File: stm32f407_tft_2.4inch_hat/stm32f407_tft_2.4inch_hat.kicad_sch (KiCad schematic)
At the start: 6 parts, among them P1 STM32F407-DISC P1, P2 STM32F407-DISC P2, U1 TFT SPI 240x320

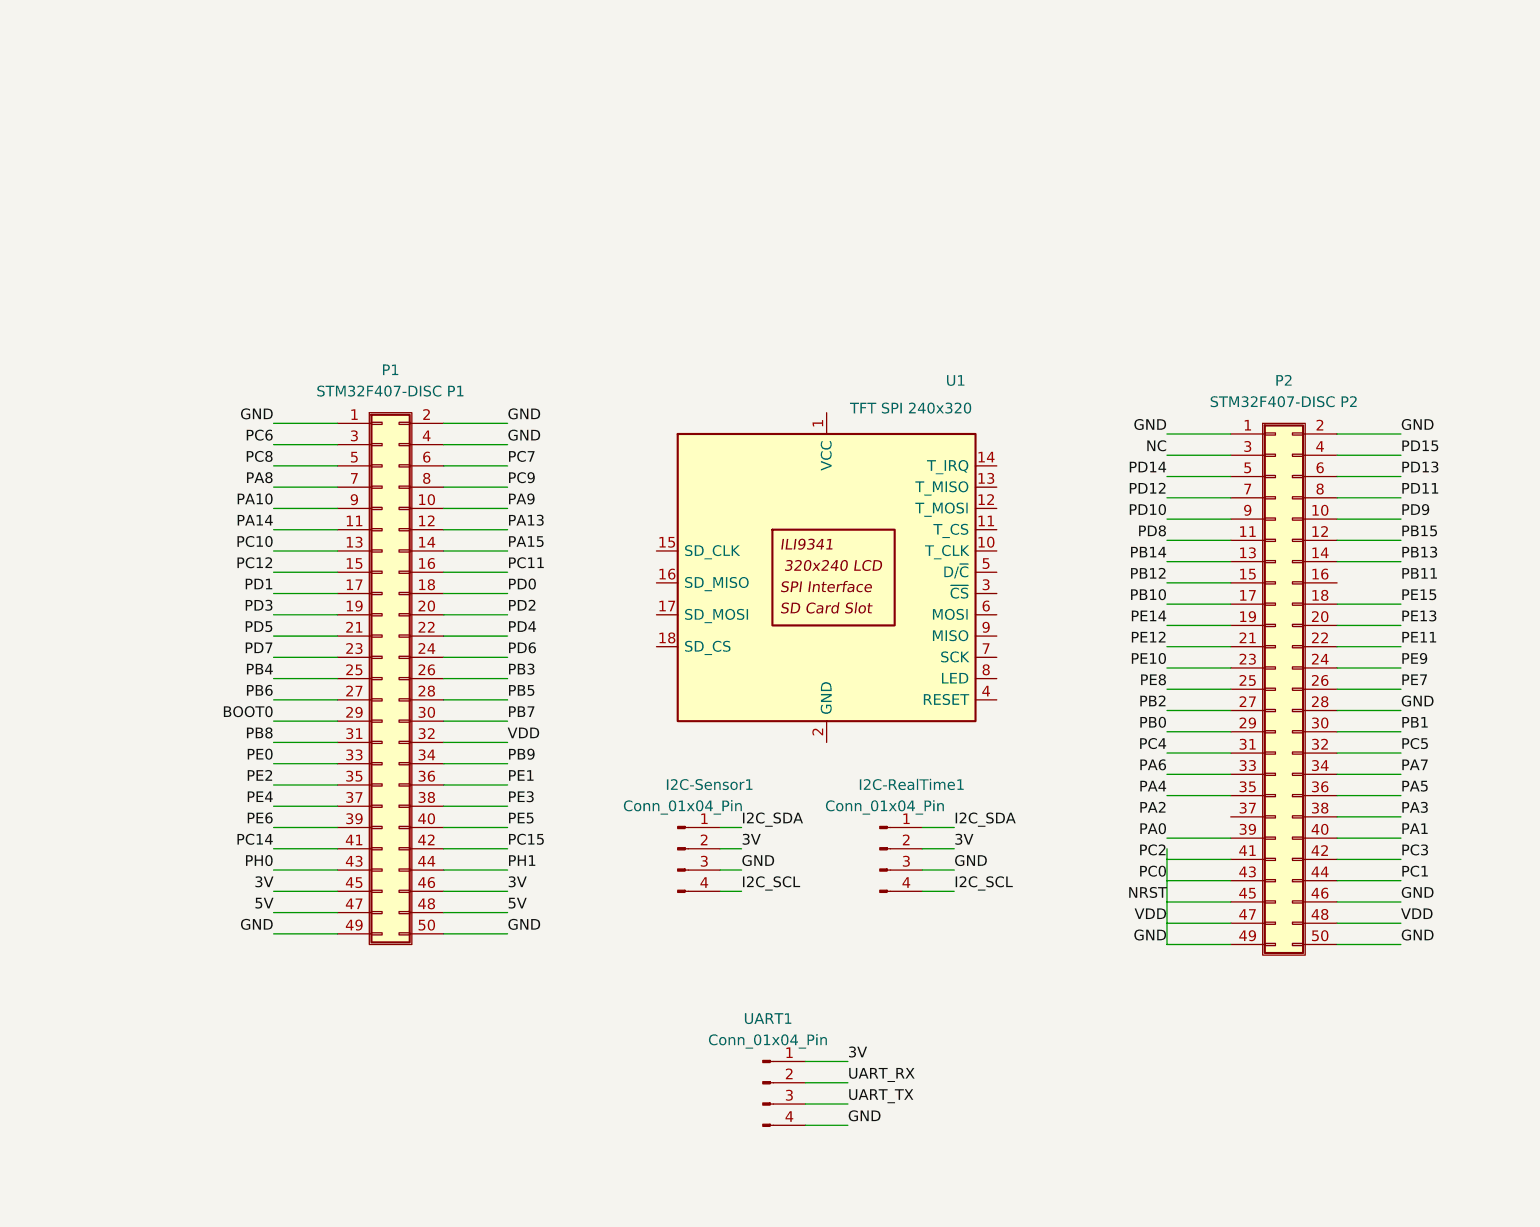
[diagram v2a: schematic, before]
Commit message: Wire i2c2 and tft
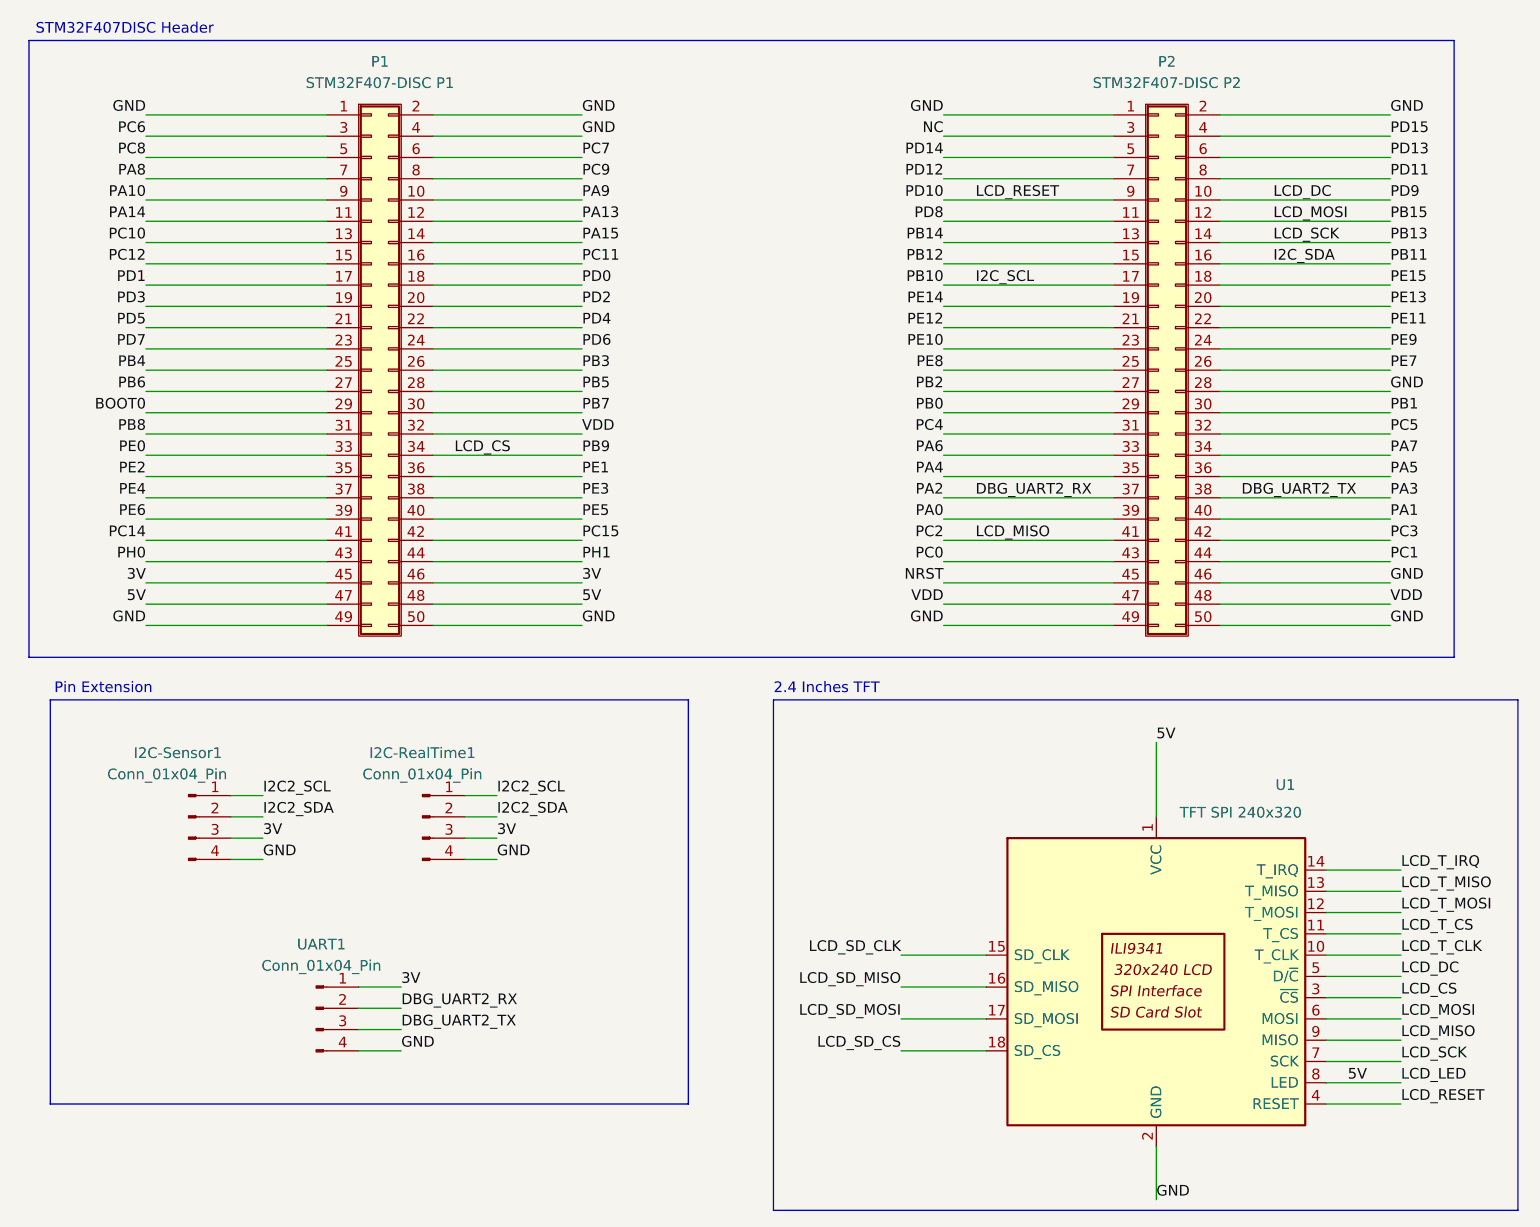
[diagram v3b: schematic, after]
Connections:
- net PB10 is gone; now on net I2C_SCL: P2.17 (PA6)
- net PB13 is gone; now on net LCD_SCK: P2.14 (PA3)
- net PB15 is gone; now on net LCD_MOSI: P2.12 (PA1)
- net PB9 is gone; now on net LCD_CS: P1.34 (PD0)
- net PD10 is gone; now on net LCD_RESET: P2.9 (PC2)
- net PD9 is gone; now on net LCD_DC: P2.10 (PC3)
- net UART_RX is gone; now on net DBG_UART2_RX: UART1.2 (Pin_2)
- net UART_TX is gone; now on net DBG_UART2_TX: UART1.3 (Pin_3)
- net 3V: now also I2C-RealTime1.3 (Pin_3), I2C-Sensor1.3 (Pin_3); no longer I2C-RealTime1.2 (Pin_2), I2C-Sensor1.2 (Pin_2)
- net 5V: now also U1.1 (VCC), U1.8 (LED)
- net GND: now also I2C-RealTime1.4 (Pin_4), I2C-Sensor1.4 (Pin_4), U1.2 (GND); no longer I2C-RealTime1.3 (Pin_3), I2C-Sensor1.3 (Pin_3), P1.32 (PD2), P2.41 (PD10), P2.43 (PD12), P2.45 (PD14), P2.47 (NC), P2.48 (PD15)
- net I2C_SCL: no longer I2C-RealTime1.4 (Pin_4), I2C-Sensor1.4 (Pin_4)
- net I2C_SDA: now also P2.16 (PA5); no longer I2C-RealTime1.1 (Pin_1), I2C-Sensor1.1 (Pin_1)
- net LCD_T_CLK: now reaches U1.10 (T_CLK)
- net LCD_T_CS: now reaches U1.11 (T_CS)
- net LCD_T_MOSI: now reaches U1.12 (T_MOSI)
- net LCD_T_MISO: now reaches U1.13 (T_MISO)
- net LCD_T_IRQ: now reaches U1.14 (T_IRQ)
- net LCD_SD_CLK: now reaches U1.15 (SD_CLK)
- net LCD_SD_MISO: now reaches U1.16 (SD_MISO)
- net LCD_SD_MOSI: now reaches U1.17 (SD_MOSI)
- net LCD_SD_CS: now reaches U1.18 (SD_CS)
- net LCD_CS: now reaches U1.3 (~{CS})
- net LCD_RESET: now reaches U1.4 (RESET)
- net LCD_DC: now reaches U1.5 (D/~{C})
- net LCD_MOSI: now reaches U1.6 (MOSI)
- net LCD_SCK: now reaches U1.7 (SCK)
- net LCD_MISO: now reaches U1.9 (MISO)
- net LCD_MISO: now also P2.41 (PD10)
- net DBG_UART2_RX: now reaches P2.37 (PB14)
- net PA3 renamed DBG_UART2_TX
- new net I2C2_SCL: I2C-RealTime1.1 (Pin_1), I2C-Sensor1.1 (Pin_1)
- new net I2C2_SDA: I2C-RealTime1.2 (Pin_2), I2C-Sensor1.2 (Pin_2)
- new net NRST: P2.45 (PD14)
- new net PC0: P2.43 (PD12)
- new net VDD: P1.32 (PD2), P2.47 (NC), P2.48 (PD15)
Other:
- note added: "2.4 Inches TFT"
- note added: "Pin Extension"
- note added: "STM32F407DISC Header"
- moved on the sheet: I2C-RealTime1, I2C-Sensor1, P1, P2, U1, UART1

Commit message: Fix pinout pcb & sch are not correct
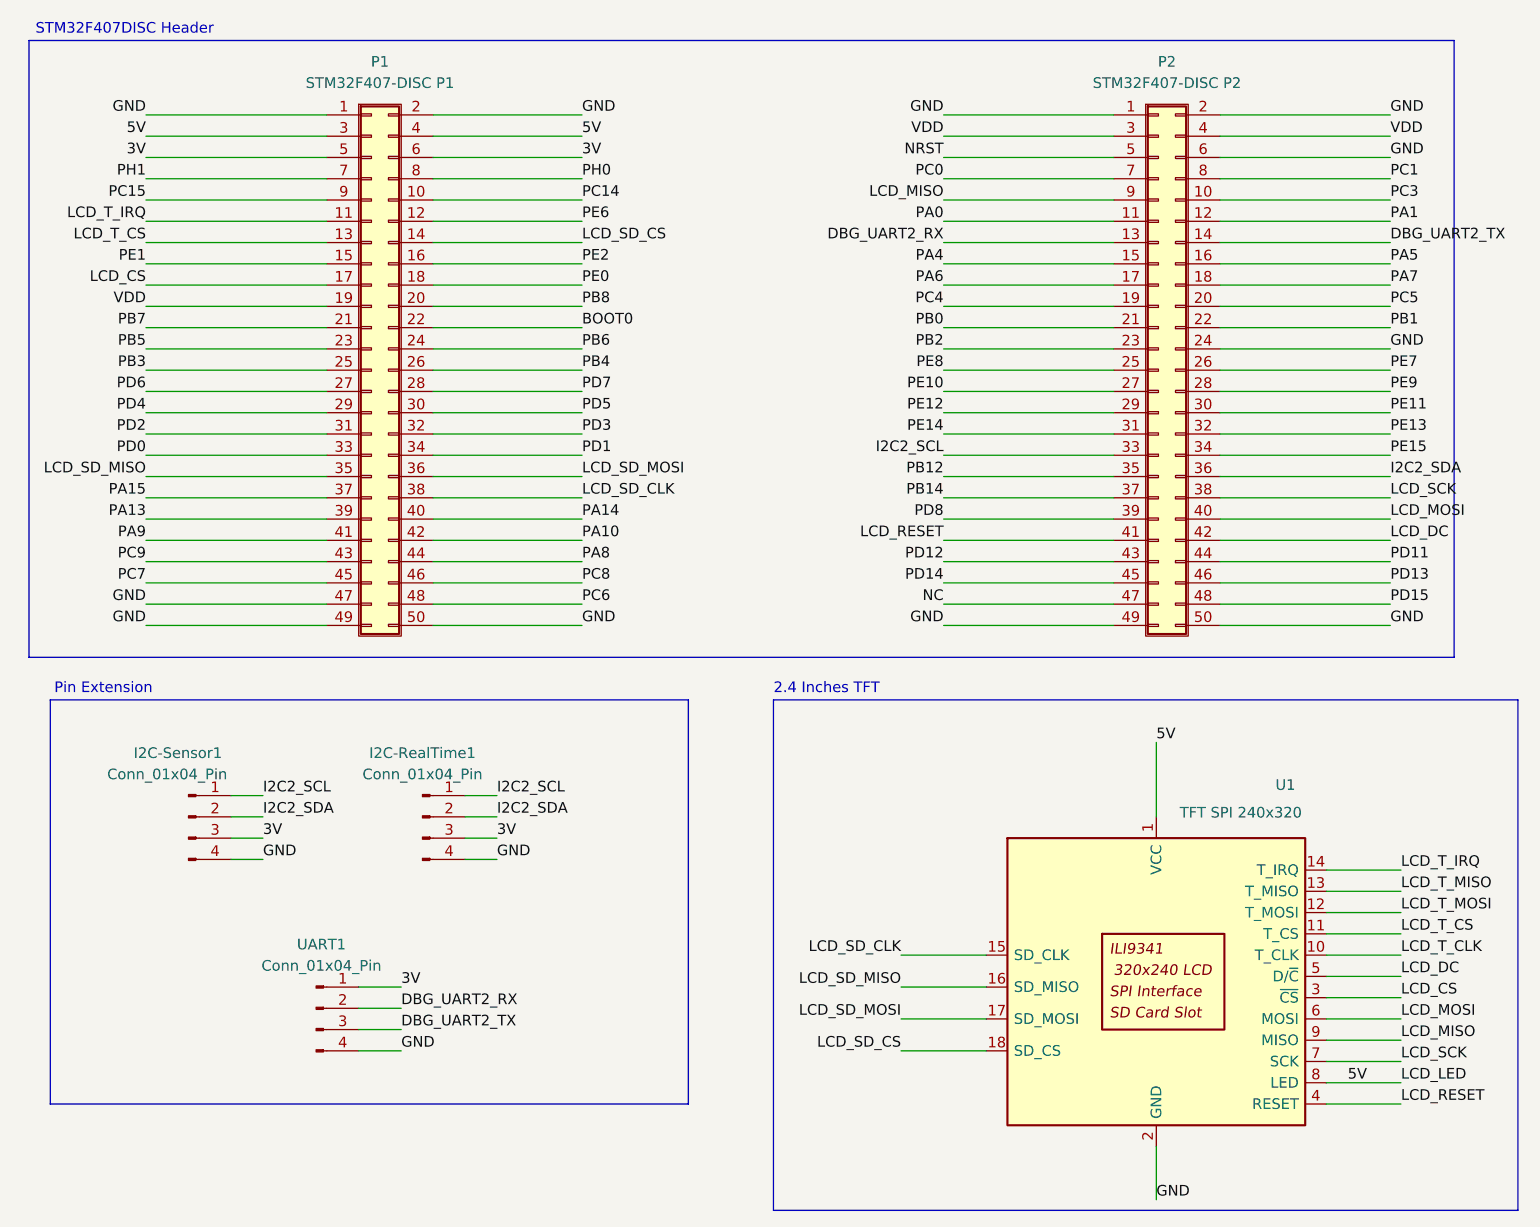
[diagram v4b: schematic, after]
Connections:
- net I2C_SCL is gone; now on net PA6: P2.17 (PA6)
- net I2C_SDA is gone; now on net PA5: P2.16 (PA5)
- net PC10 is gone; now on net LCD_T_CS: P1.13 (PE4)
- net PC11 is gone; now on net PE2: P1.16 (PE1)
- net PC12 is gone; now on net PE1: P1.15 (PE2)
- net PE3 is gone; now on net LCD_SD_CLK: P1.38 (PA15)
- net PE4 is gone; now on net PA15: P1.37 (PC10)
- net PE5 is gone; now on net PA14: P1.40 (PA13)
- net 3V: now also P1.5 (3V), P1.6 (3V); no longer P1.45 (PC8), P1.46 (PC7)
- net 5V: now also P1.3 (5V), P1.4 (5V); no longer P1.47 (PC6), P1.48 (GND)
- net BOOT0: now also P1.22 (PB7); no longer P1.29 (PD5)
- net DBG_UART2_RX: now also P2.13 (PA2); no longer P2.37 (PB14)
- net DBG_UART2_TX: now also P2.14 (PA3); no longer P2.38 (PB13)
- net GND: now also P1.47 (PC6), P2.24 (GND), P2.6 (GND); no longer P1.4 (5V), P2.28 (PE9), P2.46 (PD13)
- net I2C2_SCL: now also P2.33 (PB10)
- net I2C2_SDA: now also P2.36 (PB11)
- net LCD_CS: now also P1.17 (PE0); no longer P1.34 (PD0)
- net LCD_DC: now also P2.42 (PD9); no longer P2.10 (PC3)
- net LCD_MISO: now also P2.9 (PC2); no longer P2.41 (PD10)
- net LCD_MOSI: now also P2.40 (PB15); no longer P2.12 (PA1)
- net LCD_RESET: now also P2.41 (PD10); no longer P2.9 (PC2)
- net LCD_SCK: now also P2.38 (PB13); no longer P2.14 (PA3)
- net LCD_SD_CS: now also P1.14 (PE3)
- net LCD_SD_MISO: now also P1.35 (PC12)
- net LCD_SD_MOSI: now also P1.36 (PC11)
- net LCD_T_IRQ: now also P1.11 (PE6)
- net NC: now also P2.47 (NC); no longer P2.3 (VDD)
- net NRST: now also P2.5 (NRST); no longer P2.45 (PD14)
- net PA0: now also P2.11 (PA0); no longer P2.39 (PD8)
- net PA1: now also P2.12 (PA1); no longer P2.40 (PB15)
- net PA10: now also P1.42 (PA9); no longer P1.9 (PC14)
- net PA13: now also P1.39 (PA14); no longer P1.12 (PE5)
- net PA14: no longer P1.11 (PE6)
- net PA15: no longer P1.14 (PE3)
- net PA4: now also P2.15 (PA4); no longer P2.35 (PB12)
- net PA5: no longer P2.36 (PB11)
- net PA6: no longer P2.33 (PB10)
- net PA7: now also P2.18 (PA7); no longer P2.34 (PE15)
- net PA8: now also P1.44 (PC9); no longer P1.7 (PH0)
- net PA9: now also P1.41 (PA10); no longer P1.10 (PC15)
- net PB0: now also P2.21 (PB0); no longer P2.29 (PE12)
- net PB1: now also P2.22 (PB1); no longer P2.30 (PE11)
- net PB12: now also P2.35 (PB12); no longer P2.15 (PA4)
- net PB14: now also P2.37 (PB14); no longer P2.13 (PA2)
- net PB2: now also P2.23 (PB2); no longer P2.27 (PE10)
- net PB3: now also P1.25 (PB4); no longer P1.26 (PB3)
- net PB4: now also P1.26 (PB3); no longer P1.25 (PB4)
- net PB5: now also P1.23 (PB6); no longer P1.28 (PD6)
- net PB6: now also P1.24 (PB5); no longer P1.27 (PD7)
- net PB7: now also P1.21 (BOOT0); no longer P1.30 (PD4)
- net PB8: now also P1.20 (VDD); no longer P1.31 (PD3)
- net PC0: now also P2.7 (PC0); no longer P2.43 (PD12)
- net PC1: now also P2.8 (PC1); no longer P2.44 (PD11)
- net PC14: now also P1.10 (PC15); no longer P1.41 (PA10)
- net PC15: now also P1.9 (PC14); no longer P1.42 (PA9)
- net PC3: now also P2.10 (PC3); no longer P2.42 (PD9)
- net PC4: now also P2.19 (PC4); no longer P2.31 (PE14)
- net PC5: now also P2.20 (PC5); no longer P2.32 (PE13)
- net PC6: now also P1.48 (GND); no longer P1.3 (5V)
- net PC7: now also P1.45 (PC8); no longer P1.6 (3V)
- net PC8: now also P1.46 (PC7); no longer P1.5 (3V)
- net PC9: now also P1.43 (PA8); no longer P1.8 (PH1)
- net PD0: now also P1.33 (PD1); no longer P1.18 (PB9)
- net PD1: now also P1.34 (PD0); no longer P1.17 (PE0)
- net PD11: now also P2.44 (PD11); no longer P2.8 (PC1)
- net PD12: now also P2.43 (PD12); no longer P2.7 (PC0)
- net PD13: now also P2.46 (PD13); no longer P2.6 (GND)
- net PD14: now also P2.45 (PD14); no longer P2.5 (NRST)
- net PD15: now also P2.48 (PD15); no longer P2.4 (VDD)
- net PD2: now also P1.31 (PD3); no longer P1.20 (VDD)
- net PD3: now also P1.32 (PD2); no longer P1.19 (PB8)
- net PD4: now also P1.29 (PD5); no longer P1.22 (PB7)
- net PD5: now also P1.30 (PD4); no longer P1.21 (BOOT0)
- net PD6: now also P1.27 (PD7); no longer P1.24 (PB5)
- net PD7: now also P1.28 (PD6); no longer P1.23 (PB6)
- net PD8: now also P2.39 (PD8); no longer P2.11 (PA0)
- net PE0: now also P1.18 (PB9); no longer P1.33 (PD1)
- net PE1: no longer P1.36 (PC11)
- net PE10: now also P2.27 (PE10); no longer P2.23 (PB2)
- net PE11: now also P2.30 (PE11); no longer P2.22 (PB1)
- net PE12: now also P2.29 (PE12); no longer P2.21 (PB0)
- net PE13: now also P2.32 (PE13); no longer P2.20 (PC5)
- net PE14: now also P2.31 (PE14); no longer P2.19 (PC4)
- net PE15: now also P2.34 (PE15); no longer P2.18 (PA7)
- net PE2: no longer P1.35 (PC12)
- net PE6: now also P1.12 (PE5); no longer P1.39 (PA14)
- net PE9: now also P2.28 (PE9); no longer P2.24 (GND)
- net PH0: now also P1.8 (PH1); no longer P1.43 (PA8)
- net PH1: now also P1.7 (PH0); no longer P1.44 (PC9)
- net VDD: now also P1.19 (PB8), P2.3 (VDD), P2.4 (VDD); no longer P1.32 (PD2), P2.47 (NC), P2.48 (PD15)

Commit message: PCB wired
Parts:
- renumbered U1 to LCD_Panel1
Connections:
- net LCD_T_CLK is gone; now on net LCD_SD_CLK: LCD_Panel1.10 (T_CLK)
- net LCD_T_MISO is gone; now on net LCD_SD_MISO: LCD_Panel1.13 (T_MISO)
- net LCD_T_MOSI is gone; now on net LCD_SD_MOSI: LCD_Panel1.12 (T_MOSI)
- net GND: no longer P1.47 (PC6)
- net LCD_CS: now also P1.19 (PB8); no longer P1.17 (PE0)
- net LCD_SD_MISO: now also P1.37 (PC10); no longer P1.35 (PC12)
- net LCD_T_CS: now also P1.15 (PE2); no longer P1.13 (PE4)
- net LCD_T_IRQ: now also P1.13 (PE4); no longer P1.11 (PE6)
- net PA13: now also P1.41 (PA10); no longer P1.39 (PA14)
- net PA15: now also P1.39 (PA14); no longer P1.37 (PC10)
- net PA9: now also P1.43 (PA8); no longer P1.41 (PA10)
- net PB3: now also P1.27 (PD7); no longer P1.25 (PB4)
- net PB5: now also P1.25 (PB4); no longer P1.23 (PB6)
- net PB7: now also P1.23 (PB6); no longer P1.21 (BOOT0)
- net PC7: now also P1.47 (PC6); no longer P1.45 (PC8)
- net PC9: now also P1.45 (PC8); no longer P1.43 (PA8)
- net PD0: now also P1.35 (PC12); no longer P1.33 (PD1)
- net PD2: now also P1.33 (PD1); no longer P1.31 (PD3)
- net PD4: now also P1.31 (PD3); no longer P1.29 (PD5)
- net PD6: now also P1.29 (PD5); no longer P1.27 (PD7)
- net PE1: now also P1.17 (PE0); no longer P1.15 (PE2)
- net VDD: no longer P1.19 (PB8)
- new net PC13: P1.11 (PE6)

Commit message: Final state and export gerber
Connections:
- net DBG_UART2_RX: now also P2.14 (PA3); no longer P2.13 (PA2)
- net DBG_UART2_TX: now also P2.13 (PA2); no longer P2.14 (PA3)
